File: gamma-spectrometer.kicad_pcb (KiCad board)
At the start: 2 copper layers, 123.5 x 55 mm, 80 parts, among them J1 *, J2 *, J3 *, J4 *, J5 *, J6 *, Q1 2N7002, Q2 2N7002, Q3 MMBT5088LT1G, Q4 MMBT5088LT1G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

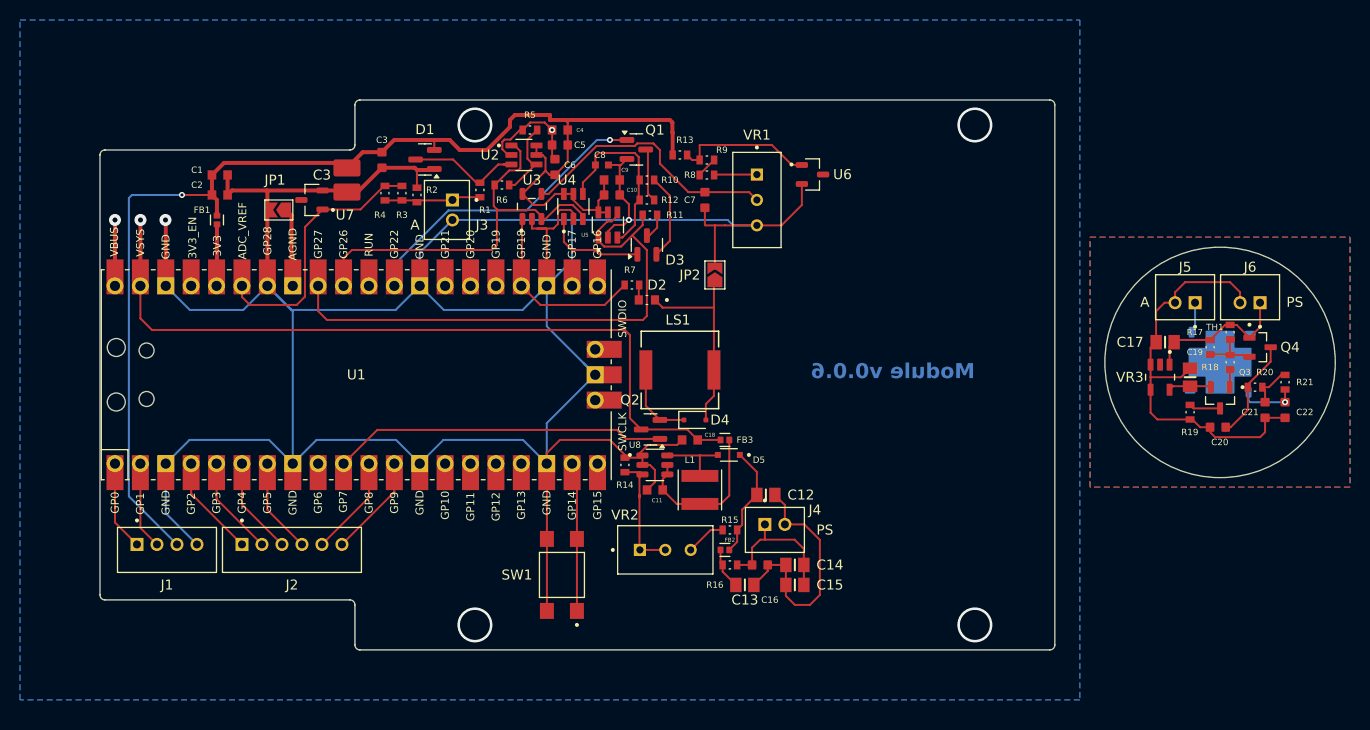
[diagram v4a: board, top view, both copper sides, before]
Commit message: PCB size fix
PCB size fix
Zoomer position adjustment
Minor fixes

Centered U1

PCB view update
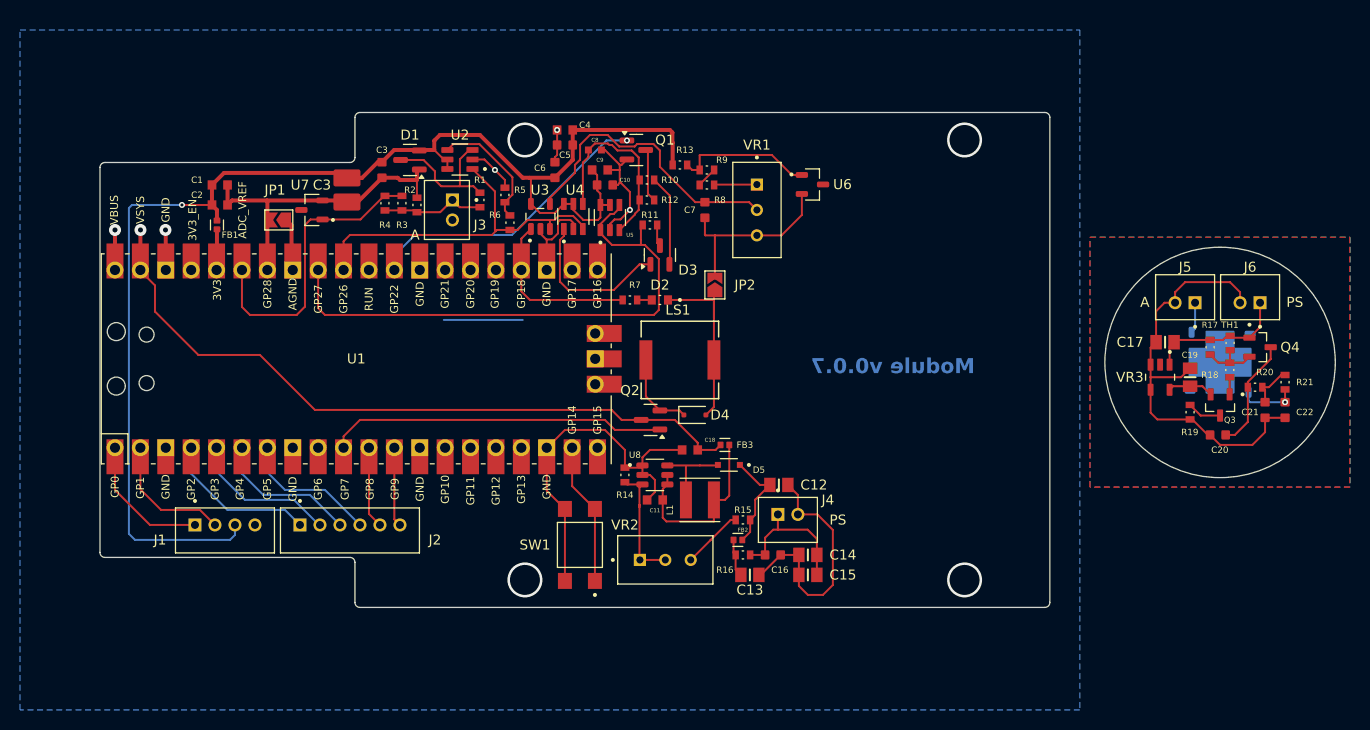
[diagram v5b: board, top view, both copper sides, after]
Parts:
- moved R5 6.96 mm to (128.5, 67.5), turned to -90 degrees
- moved U2 6.42 mm to (124.0, 64.0), turned to 180 degrees
- moved J1 6.12 mm to (100.5, 101.0)
- moved J2 6.12 mm to (113.0, 101.0)
- moved R6 3.86 mm to (129.0, 70.3), turned to -90 degrees
- moved SW1 3.50 mm to (136.0, 102.5)
- moved C8 1.66 mm to (137.5, 63.0)
- moved C12 1.64 mm to (155.9, 96.5)
- moved C14 1.64 mm to (158.8, 103.5)
- moved C15 1.64 mm to (158.8, 105.5)
- moved C16 1.64 mm to (155.3, 103.5)
- moved D3 1.64 mm to (144.0, 73.5)
- moved FB2 1.64 mm to (151.8, 102.0)
- moved J4 1.64 mm to (156.8, 100.0)
- moved R15 1.64 mm to (152.3, 100.0)
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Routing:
- net GND: track 346.4 -> 155.2 mm, vias 3 -> 4
- net +5V: track 77.8 -> 71.8 mm
- net Net-(D3-A): track 10.2 -> 15.9 mm
- net SIG: track 42.4 -> 36.7 mm
- net SCK: track 10.2 -> 15.6 mm
- net UART1RX: track 10.3 -> 5.36 mm
- net RX: track 9.74 -> 14.5 mm
- net Net-(U2--IN): track 8.00 -> 12.5 mm
- net UART1TX: track 10.0 -> 5.59 mm
- net TX: track 10.5 -> 14.9 mm
- net CS: track 9.51 -> 13.9 mm
- net Net-(U1-GPIO14): track 14.9 -> 11.7 mm
- net VREF: track 26.4 -> 29.7 mm
- net INT: track 20.3 -> 17.1 mm
- net Net-(D1-COM): track 11.5 -> 14.5 mm
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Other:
- board size 123.5 x 55 mm -> 123.5 x 49.5 mm
- board text added: "Module v0.0.7"
- board text removed: "Module v0.0.6"

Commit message: C3 duplication fix
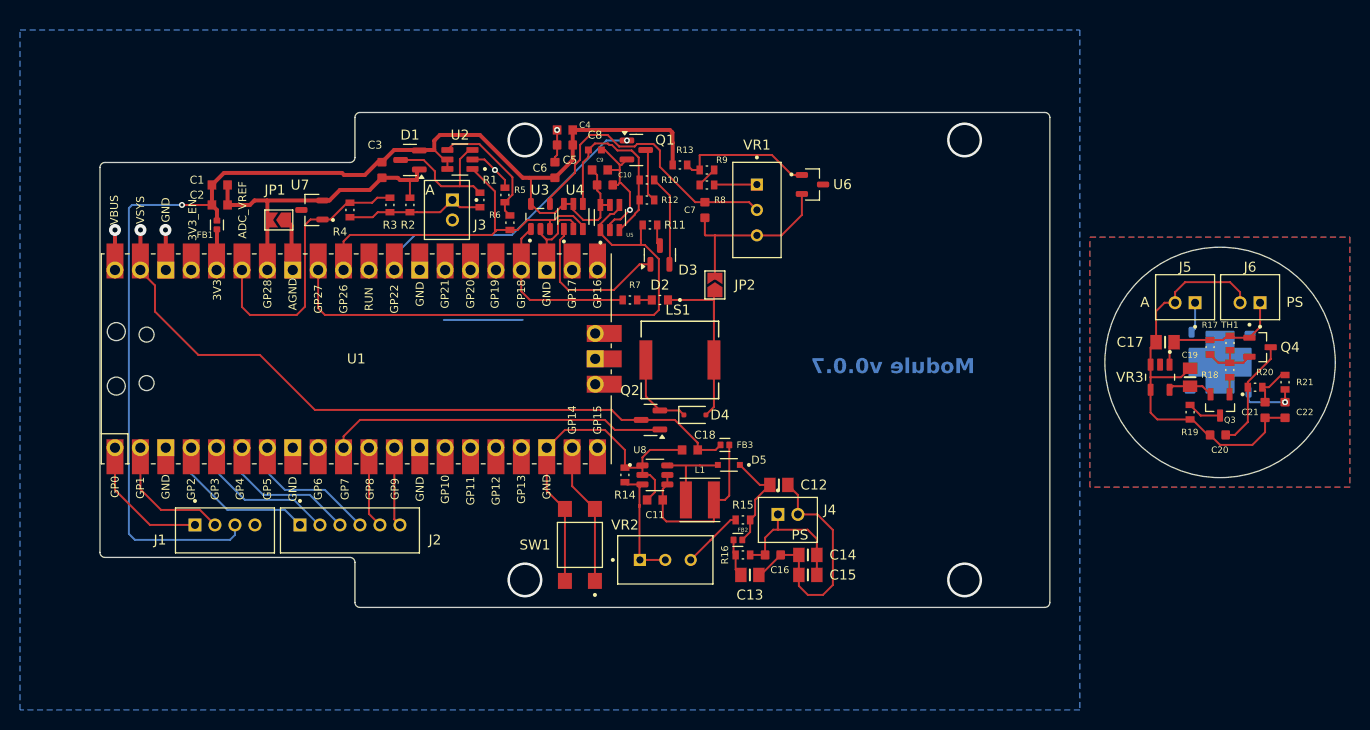
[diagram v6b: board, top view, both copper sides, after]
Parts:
- removed the C3 at (112.7, 67.0)
- FB1, FB3: value 1k -> BLM18KG102SN1D
- FB2: value ACML-0402HC-301-T -> BLM18KG102SN1D
- moved R4 3.57 mm to (113.0, 69.0)
- moved R3 1.21 mm to (117.0, 68.5)
- moved R2 0.70 mm to (119.0, 68.5)
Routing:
- net ANODE_IN: track 10.4 -> 14.0 mm
- net VREF: track 29.7 -> 28.4 mm

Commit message: Changed schematic for default I2C pins
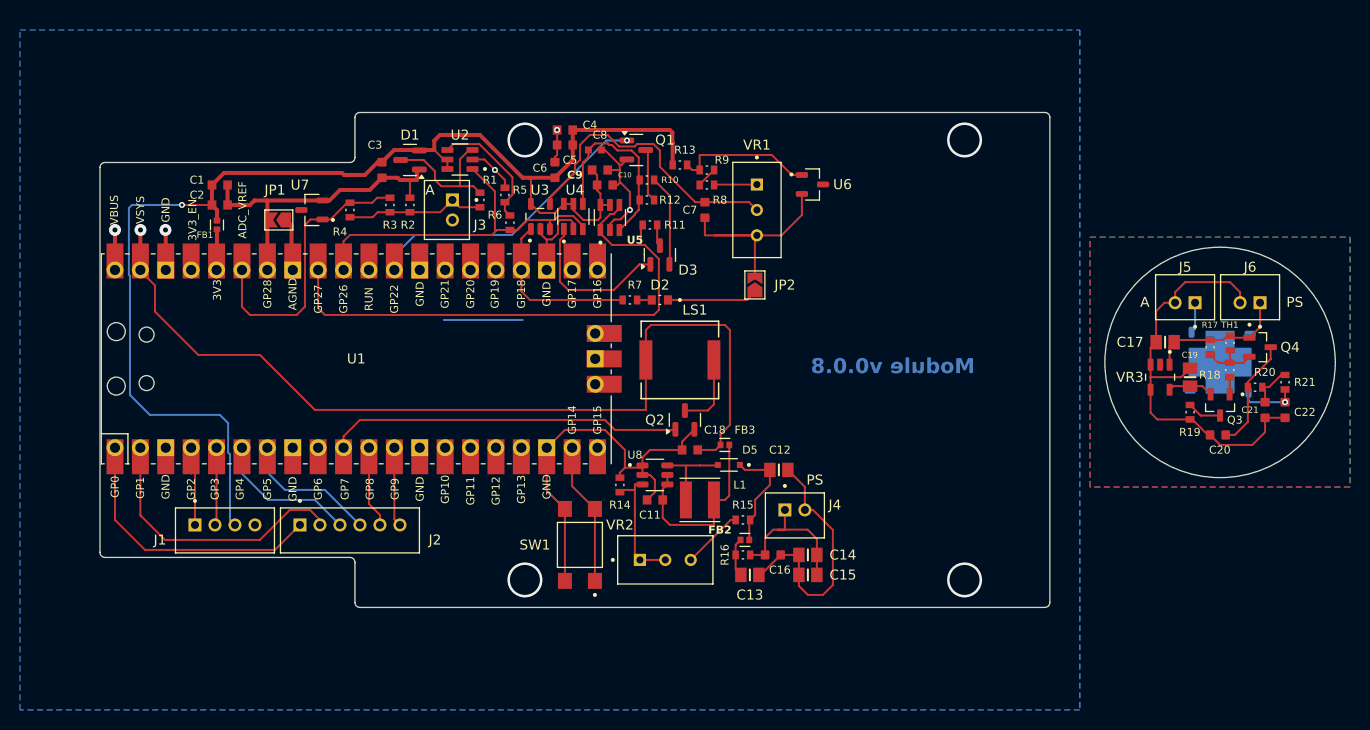
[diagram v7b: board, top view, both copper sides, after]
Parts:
- removed D4: PMEG4010BEA,115, Diode_SMD:D_SOD-323F
- moved JP2 4.00 mm to (153.5, 76.5)
- moved Q2 3.44 mm to (146.5, 90.0), turned to 90 degrees
- moved C12 1.50 mm to (155.9, 95.0)
- moved R14 1.12 mm to (140.0, 96.5)
- moved J4 0.83 mm to (157.5, 99.5)
- moved FB2 0.70 mm to (152.5, 102.0)
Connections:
- LS1 pad 1: Net-(D4-K) -> +5V
- LS1 pad 2: IND -> Net-(Q2-D)
- Q2 pad 2: Net-(D4-K) -> GND
- Q2 pad 3: +5V -> Net-(Q2-D)
- U1 pad 1: SDA -> SCK
- U1 pad 2: SCL -> TX
- U1 pad 4: SCK -> SDA
- U1 pad 5: TX -> SCL
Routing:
- net +5V: track 71.8 -> 93.2 mm
- net TX: track 14.9 -> 28.0 mm
- net SCK: track 15.6 -> 28.0 mm
- net IND: track 19.6 -> 9.01 mm
- net GND: track 155.1 -> 163.4 mm
- net Net-(D4-K): track 8.22 -> 0.00 mm
- net Net-(Q2-D): track 0.00 -> 7.60 mm
- net VCC: track 134.8 -> 130.3 mm
- net TCKR: track 34.0 -> 35.5 mm
- net PS_OUT: track 14.2 -> 15.4 mm
- net Net-(U8-FB): track 12.3 -> 13.2 mm
- net SDA: track 11.1 -> 10.5 mm
- net Net-(D5-K): track 10.5 -> 11.1 mm
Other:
- board text added: "Module v0.0.8"
- board text removed: "Module v0.0.7"
